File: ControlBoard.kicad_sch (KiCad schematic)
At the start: 9 parts, among them J11 5x2.54mm+2xBus, J13 AudioJack3, J14 USBCPD, U2 LMC6484IN_NOPB, U5 ESP32-C6-DEVKITC-1-N8

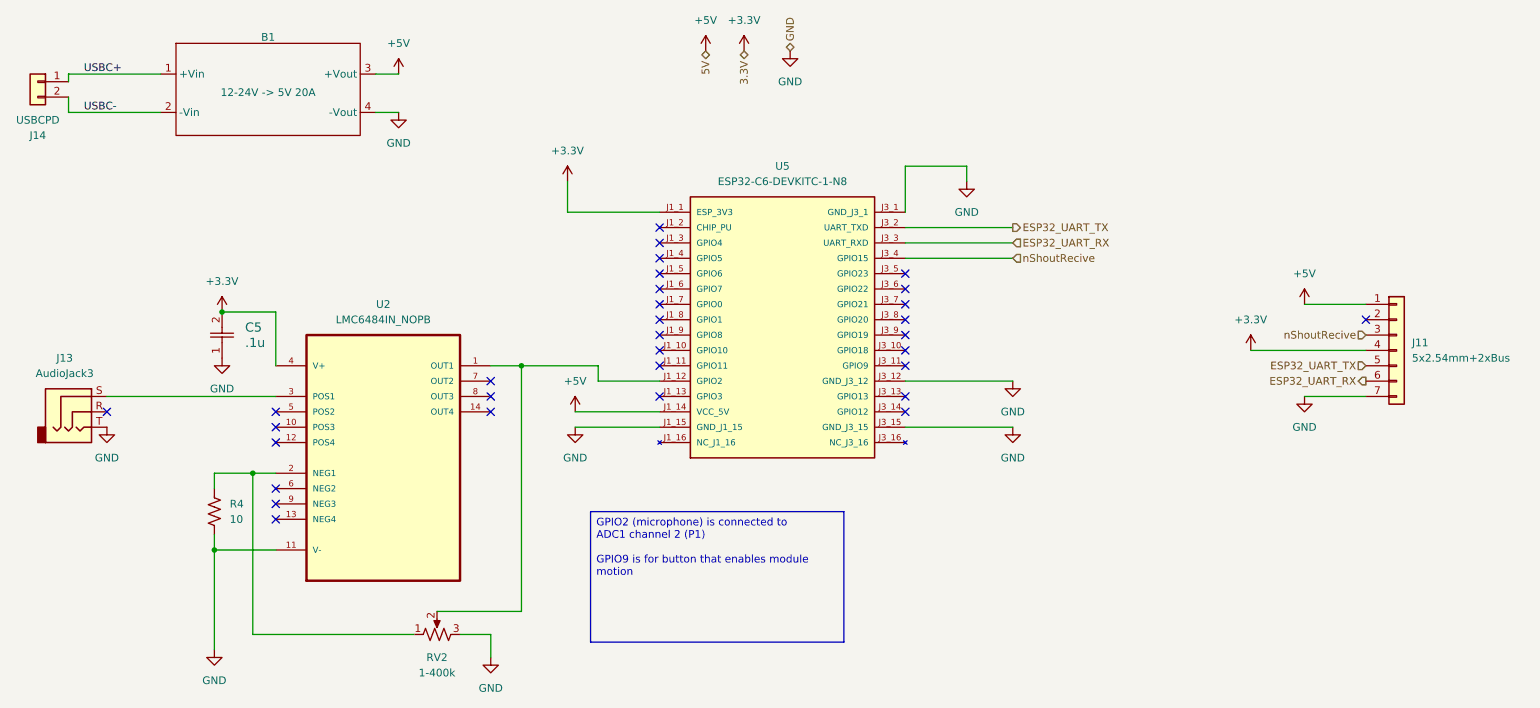
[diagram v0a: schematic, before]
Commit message: Refrences Changed, Root file fixed, UART Note Added
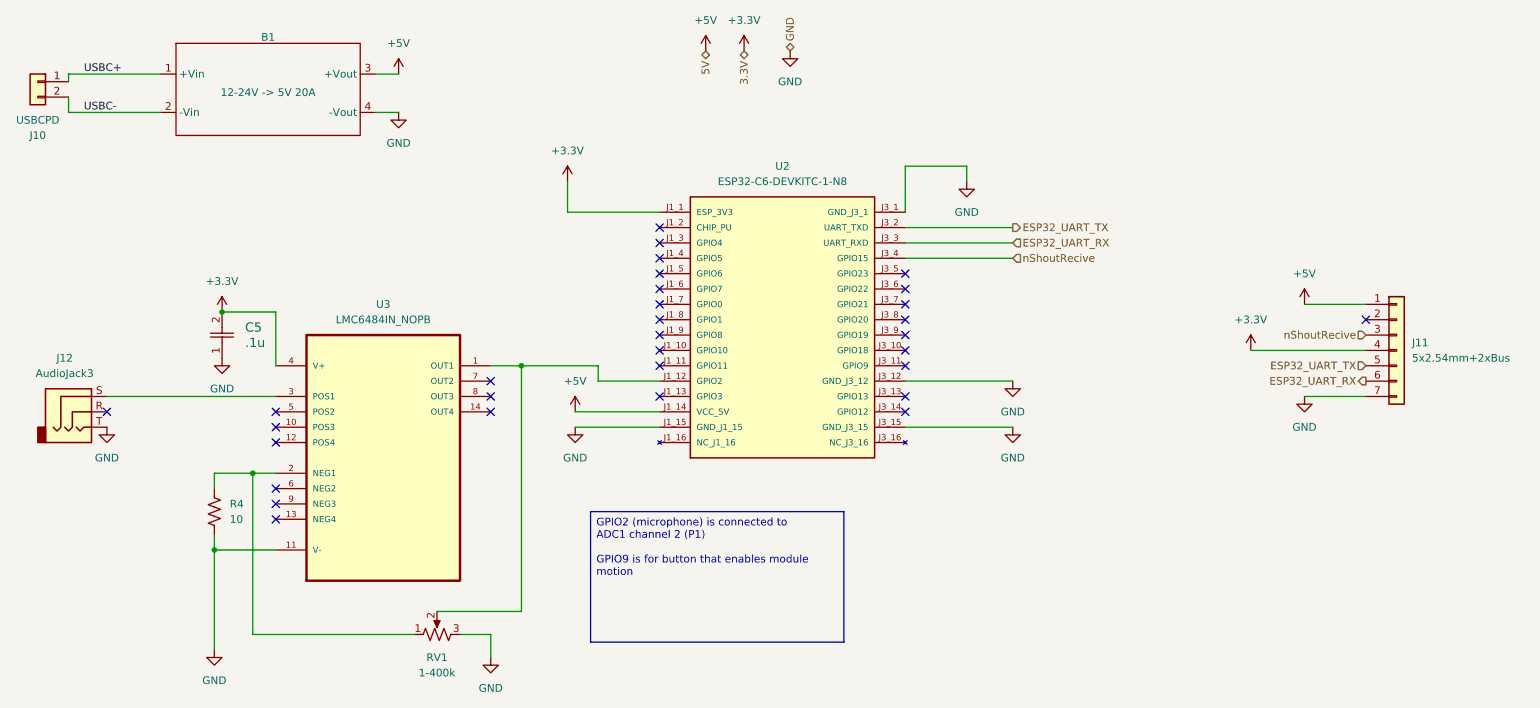
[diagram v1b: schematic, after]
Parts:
- renumbered J14 to J10, J13 to J12, RV2 to RV1, U5 to U2, U2 to U3
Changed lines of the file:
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@@
 		(dnp no)
 		(fields_autoplaced yes)
-		(property "Reference" "RV2"
+		(property "Reference" "RV1"
 			(at 92.71 130.81 90)
 			(effects
@@
 			(project "ECE 2799 Rose Actuator Boards V2"
 				(path "/7b54b20f-95ea-471b-884f-de37eca32e63/680dcb38-59ad-40f5-9cf6-60f2a89c70fa"
-					(reference "RV2")
+					(reference "RV1")
 					(unit 1)
 				)
@@
 		(on_board yes)
 		(dnp no)
-		(property "Reference" "#PWR029"
+		(property "Reference" "#PWR023"
 			(at 114.3 55.88 0)
 			(effects
@@
 			(project "ECE 2799 Rose Actuator Boards V2"
 				(path "/7b54b20f-95ea-471b-884f-de37eca32e63/680dcb38-59ad-40f5-9cf6-60f2a89c70fa"
-					(reference "#PWR029")
+					(reference "#PWR023")
 					(unit 1)
 				)
@@
 		(dnp no)
 		(fields_autoplaced yes)
-		(property "Reference" "#PWR030"
+		(property "Reference" "#PWR031"
 			(at 115.57 93.98 0)
 			(effects
@@
 			(project "ECE 2799 Rose Actuator Boards V2"
 				(path "/7b54b20f-95ea-471b-884f-de37eca32e63/680dcb38-59ad-40f5-9cf6-60f2a89c70fa"
-					(reference "#PWR030")
+					(reference "#PWR031")
 					(unit 1)
 				)
@@
 		(dnp no)
 		(fields_autoplaced yes)
-		(property "Reference" "J13"
+		(property "Reference" "J12"
 			(at 31.115 81.28 0)
 			(effects
@@
 			(project ""
 				(path "/7b54b20f-95ea-471b-884f-de37eca32e63/680dcb38-59ad-40f5-9cf6-60f2a89c70fa"
-					(reference "J13")
+					(reference "J12")
 					(unit 1)
 				)
@@
 		(on_board yes)
 		(dnp no)
-		(property "Reference" "#PWR027"
+		(property "Reference" "#PWR026"
 			(at 57.15 77.47 0)
 			(effects
@@
 			(project "ECE 2799 Rose Actuator Boards V2"
 				(path "/7b54b20f-95ea-471b-884f-de37eca32e63/680dcb38-59ad-40f5-9cf6-60f2a89c70fa"
-					(reference "#PWR027")
+					(reference "#PWR026")
 					(unit 1)
 				)
@@
 		(dnp no)
 		(fields_autoplaced yes)
-		(property "Reference" "#PWR035"
+		(property "Reference" "#PWR032"
 			(at 38.1 99.06 0)
 			(effects
@@
 			(project ""
 				(path "/7b54b20f-95ea-471b-884f-de37eca32e63/680dcb38-59ad-40f5-9cf6-60f2a89c70fa"
-					(reference "#PWR035")
+					(reference "#PWR032")
 					(unit 1)
 				)
@@
 		(dnp no)
 		(fields_autoplaced yes)
-		(property "Reference" "#PWR031"
+		(property "Reference" "#PWR033"
 			(at 115.57 99.06 0)
 			(effects
@@
 			(project "ECE 2799 Rose Actuator Boards V2"
 				(path "/7b54b20f-95ea-471b-884f-de37eca32e63/680dcb38-59ad-40f5-9cf6-60f2a89c70fa"
-					(reference "#PWR031")
+					(reference "#PWR033")
 					(unit 1)
 				)
@@
 		(dnp no)
 		(fields_autoplaced yes)
-		(property "Reference" "#PWR09"
+		(property "Reference" "#PWR019"
 			(at 143.51 34.29 0)
 			(effects
@@
 			(project "ECE 2799 Rose Actuator Boards V2"
 				(path "/7b54b20f-95ea-471b-884f-de37eca32e63/680dcb38-59ad-40f5-9cf6-60f2a89c70fa"
-					(reference "#PWR09")
+					(reference "#PWR019")
 					(unit 1)
 				)
@@
 		(dnp no)
 		(fields_autoplaced yes)
-		(property "Reference" "#PWR051"
+		(property "Reference" "#PWR022"
 			(at 86.36 46.99 0)
 			(effects
@@
 			(project "ECE 2799 Rose Actuator Boards V2"
 				(path "/7b54b20f-95ea-471b-884f-de37eca32e63/680dcb38-59ad-40f5-9cf6-60f2a89c70fa"
-					(reference "#PWR051")
+					(reference "#PWR022")
 					(unit 1)
 				)
@@
 		(dnp no)
 		(fields_autoplaced yes)
-		(property "Reference" "#PWR010"
+		(property "Reference" "#PWR020"
 			(at 151.13 36.83 0)
 			(effects
@@
 			(project "ECE 2799 Rose Actuator Boards V2"
 				(path "/7b54b20f-95ea-471b-884f-de37eca32e63/680dcb38-59ad-40f5-9cf6-60f2a89c70fa"
-					(reference "#PWR010")
+					(reference "#PWR020")
 					(unit 1)
 				)
@@
 		(on_board yes)
 		(dnp no)
-		(property "Reference" "J14"
+		(property "Reference" "J10"
 			(at 26.67 44.45 0)
 			(effects
@@
 			(project ""
 				(path "/7b54b20f-95ea-471b-884f-de37eca32e63/680dcb38-59ad-40f5-9cf6-60f2a89c70fa"
-					(reference "J14")
+					(reference "J10")
 					(unit 1)
 				)
@@
 		(dnp no)
 		(fields_autoplaced yes)
-		(property "Reference" "#PWR037"
+		(property "Reference" "#PWR021"
 			(at 86.36 38.1 0)
 			(effects
@@
 			(project "ECE 2799 Rose Actuator Boards V2"
 				(path "/7b54b20f-95ea-471b-884f-de37eca32e63/680dcb38-59ad-40f5-9cf6-60f2a89c70fa"
-					(reference "#PWR037")
+					(reference "#PWR021")
 					(unit 1)
 				)
@@
 		(dnp no)
 		(fields_autoplaced yes)
-		(property "Reference" "#PWR028"
+		(property "Reference" "#PWR036"
 			(at 101.6 137.16 0)
 			(effects
@@
 			(project "ECE 2799 Rose Actuator Boards V2"
 				(path "/7b54b20f-95ea-471b-884f-de37eca32e63/680dcb38-59ad-40f5-9cf6-60f2a89c70fa"
-					(reference "#PWR028")
+					(reference "#PWR036")
 					(unit 1)
 				)
@@
 		(dnp no)
 		(fields_autoplaced yes)
-		(property "Reference" "#PWR046"
+		(property "Reference" "#PWR025"
 			(at 236.22 76.2 0)
 			(effects
@@
 			(project "ECE 2799 Rose Actuator Boards V2"
 				(path "/7b54b20f-95ea-471b-884f-de37eca32e63/680dcb38-59ad-40f5-9cf6-60f2a89c70fa"
-					(reference "#PWR046")
+					(reference "#PWR025")
 					(unit 1)
 				)
@@
 		(dnp no)
 		(fields_autoplaced yes)
-		(property "Reference" "U5"
+		(property "Reference" "U2"
 			(at 149.86 49.53 0)
 			(effects
@@
 			(project "ECE 2799 Rose Actuator Boards V2"
 				(path "/7b54b20f-95ea-471b-884f-de37eca32e63/680dcb38-59ad-40f5-9cf6-60f2a89c70fa"
-					(reference "U5")
+					(reference "U2")
 					(unit 1)
 				)
@@
 		(dnp no)
 		(fields_autoplaced yes)
-		(property "Reference" "U2"
+		(property "Reference" "U3"
 			(at 83.82 72.39 0)
 			(effects
@@
 			(project "ECE 2799 Rose Actuator Boards V2"
 				(path "/7b54b20f-95ea-471b-884f-de37eca32e63/680dcb38-59ad-40f5-9cf6-60f2a89c70fa"
-					(reference "U2")
+					(reference "U3")
 					(unit 1)
 				)
@@
 		(dnp no)
 		(fields_autoplaced yes)
-		(property "Reference" "#PWR045"
+		(property "Reference" "#PWR027"
 			(at 227.33 83.82 0)
 			(effects
@@
 			(project "ECE 2799 Rose Actuator Boards V2"
 				(path "/7b54b20f-95ea-471b-884f-de37eca32e63/680dcb38-59ad-40f5-9cf6-60f2a89c70fa"
-					(reference "#PWR045")
+					(reference "#PWR027")
 					(unit 1)
 				)
@@
 		(dnp no)
 		(fields_autoplaced yes)
-		(property "Reference" "#PWR047"
+		(property "Reference" "#PWR030"
 			(at 236.22 93.98 0)
 			(effects
@@
 			(project "ECE 2799 Rose Actuator Boards V2"
 				(path "/7b54b20f-95ea-471b-884f-de37eca32e63/680dcb38-59ad-40f5-9cf6-60f2a89c70fa"
-					(reference "#PWR047")
+					(reference "#PWR030")
 					(unit 1)
 				)
@@
 		(dnp no)
 		(fields_autoplaced yes)
-		(property "Reference" "#PWR032"
+		(property "Reference" "#PWR024"
 			(at 180.34 58.42 0)
 			(effects
@@
 			(project "ECE 2799 Rose Actuator Boards V2"
 				(path "/7b54b20f-95ea-471b-884f-de37eca32e63/680dcb38-59ad-40f5-9cf6-60f2a89c70fa"
-					(reference "#PWR032")
+					(reference "#PWR024")
 					(unit 1)
 				)
@@
 		(dnp no)
 		(fields_autoplaced yes)
-		(property "Reference" "#PWR05"
+		(property "Reference" "#PWR018"
 			(at 137.16 34.29 0)
 			(effects
@@
 			(project "ECE 2799 Rose Actuator Boards V2"
 				(path "/7b54b20f-95ea-471b-884f-de37eca32e63/680dcb38-59ad-40f5-9cf6-60f2a89c70fa"
-					(reference "#PWR05")
+					(reference "#PWR018")
 					(unit 1)
 				)
@@
 		(dnp no)
 		(fields_autoplaced yes)
-		(property "Reference" "#PWR033"
+		(property "Reference" "#PWR029"
 			(at 187.96 91.44 0)
 			(effects
@@
 			(project "ECE 2799 Rose Actuator Boards V2"
 				(path "/7b54b20f-95ea-471b-884f-de37eca32e63/680dcb38-59ad-40f5-9cf6-60f2a89c70fa"
-					(reference "#PWR033")
+					(reference "#PWR029")
 					(unit 1)
 				)
@@
 		(dnp no)
 		(fields_autoplaced yes)
-		(property "Reference" "#PWR026"
+		(property "Reference" "#PWR035"
 			(at 55.88 135.89 0)
 			(effects
@@
 			(project "ECE 2799 Rose Actuator Boards V2"
 				(path "/7b54b20f-95ea-471b-884f-de37eca32e63/680dcb38-59ad-40f5-9cf6-60f2a89c70fa"
-					(reference "#PWR026")
+					(reference "#PWR035")
 					(unit 1)
 				)
@@
 		(dnp no)
 		(fields_autoplaced yes)
-		(property "Reference" "#PWR036"
+		(property "Reference" "#PWR028"
 			(at 57.15 87.63 0)
 			(effects
@@
 			(project "ECE 2799 Rose Actuator Boards V2"
 				(path "/7b54b20f-95ea-471b-884f-de37eca32e63/680dcb38-59ad-40f5-9cf6-60f2a89c70fa"
-					(reference "#PWR036")
-					(unit 1)
-				)
+					(reference "#PWR028")
+					(unit 1)
+				)

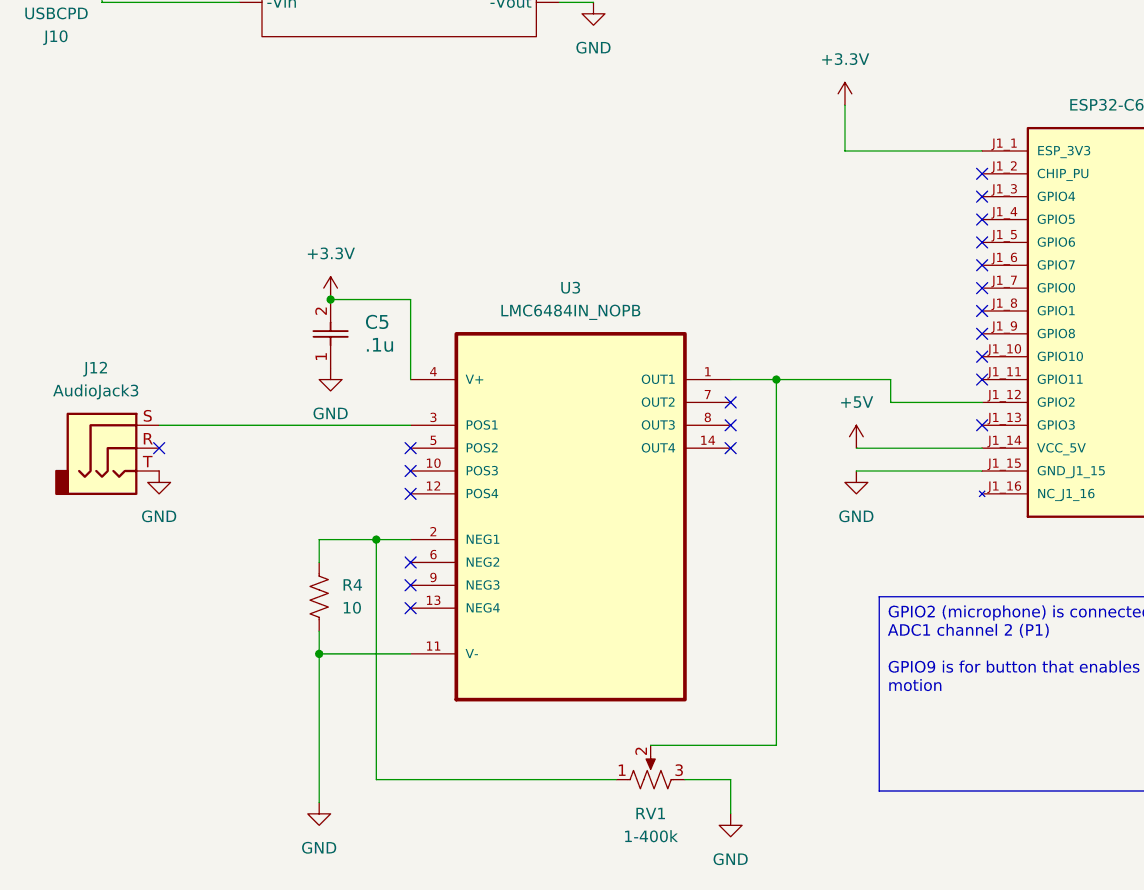
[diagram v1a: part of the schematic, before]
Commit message: Direcctory reorganization footprints added
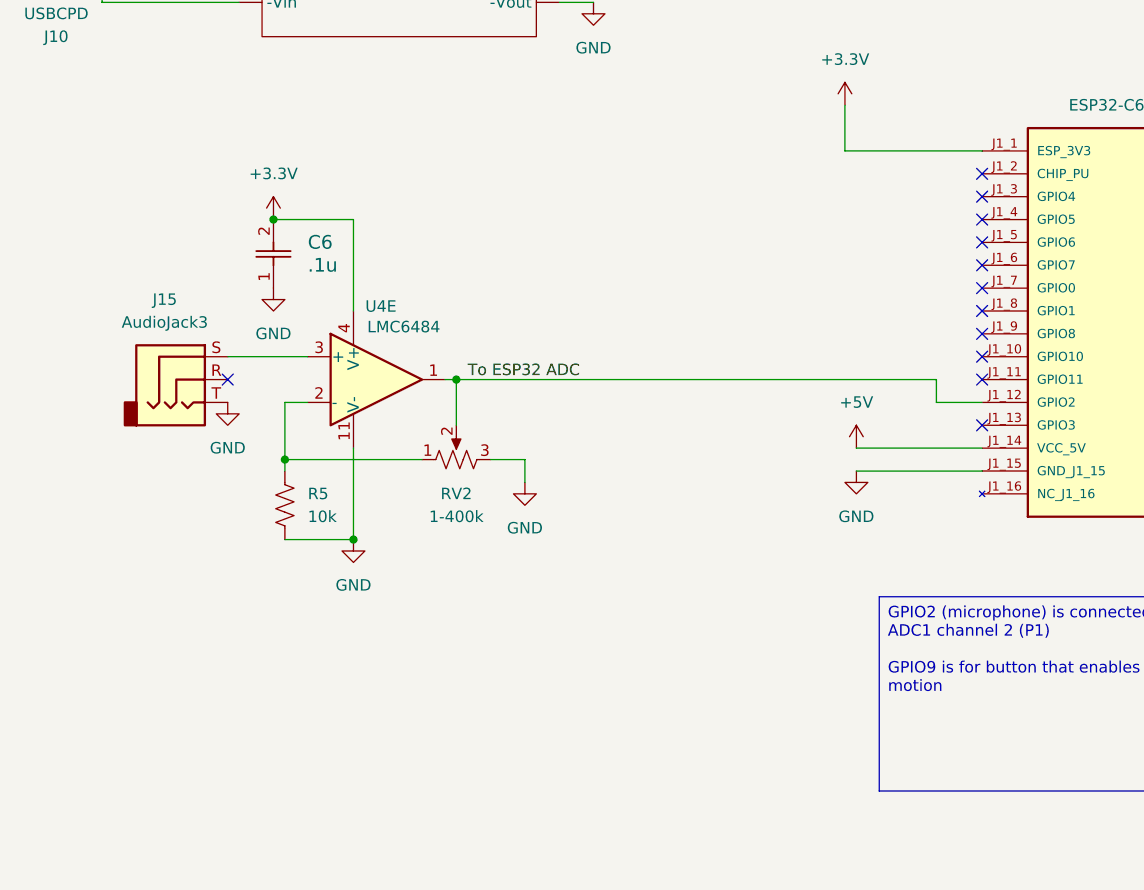
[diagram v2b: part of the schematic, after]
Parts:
- removed C5: .1u, CAPC220145_88N_KEM, symbol roseActuatorLibrary:C0805C104J5RACTU
- removed J12: AudioJack3, symbol Connector_Audio:AudioJack3
- removed R4: 10, symbol Device:R_US
- removed RV1: 1-400k, symbol Device:R_Potentiometer_US
- removed U3: LMC6484IN_NOPB, LMC6484IN_NOPB:DIP254P762X508-14, symbol roseActuatorLibrary:LMC6484IN_NOPB
- added C6: .1u, Capacitor_SMD:C_0805_2012Metric_Pad1.18x1.45mm_HandSolder, symbol roseActuatorLibrary:C0805C104J5RACTU
- added J15: AudioJack3, symbol Connector_Audio:AudioJack3
- added R5: 10k, Resistor_SMD:R_1206_3216Metric_Pad1.30x1.75mm_HandSolder, symbol Device:R_US
- added RV2: 1-400k, symbol Device:R_Potentiometer_US
- added U4: LMC6484, Rose Actuator Library:DIP254P762X508-14, symbol Amplifier_Operational:LMC6484
- J11: footprint (none) -> Rose Actuator Library:InterModuleConnectorMside
- U2: footprint ESP32-C6-DEVKITC-1-N8:MODULE_ESP32-C6-DEVKITC-1-N8 -> Rose Actuator Library:MODULE_ESP32-C6-DEVKITC-1-N8
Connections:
- net +3.3V: now also C6.2, U4.4 (V+)
- net GND: now also C6.1, J15.T, R5.2, RV2.3, U4.11 (V-)
- net To ESP32 ADC: now reaches U2.J1_12 (GPIO2)
- net To ESP32 ADC: now also RV2.2, U4.1
- new net: R5.1, RV2.1, U4.2 (-)
- new net: J15.S, U4.3 (+)
- no-connect marks 31 -> 22

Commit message: Improved amplifier
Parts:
- removed J15: AudioJack3, symbol Connector_Audio:AudioJack3
- added J12: AudioJack3, symbol Connector_Audio:AudioJack3
- added R4, R6: 40k, symbol Device:R_US
- R5: value 10k -> 50
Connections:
- net +3.3V: now also R4.1
- net GND: now also R6.2; no longer R5.2
- net at U4.3 (+): now also J12.S
- new net +1.65V: J12.T, R4.2, R5.2, R6.1
